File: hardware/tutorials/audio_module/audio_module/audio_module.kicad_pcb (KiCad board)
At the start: 2 copper layers, 25.5 x 32 mm, 5 parts

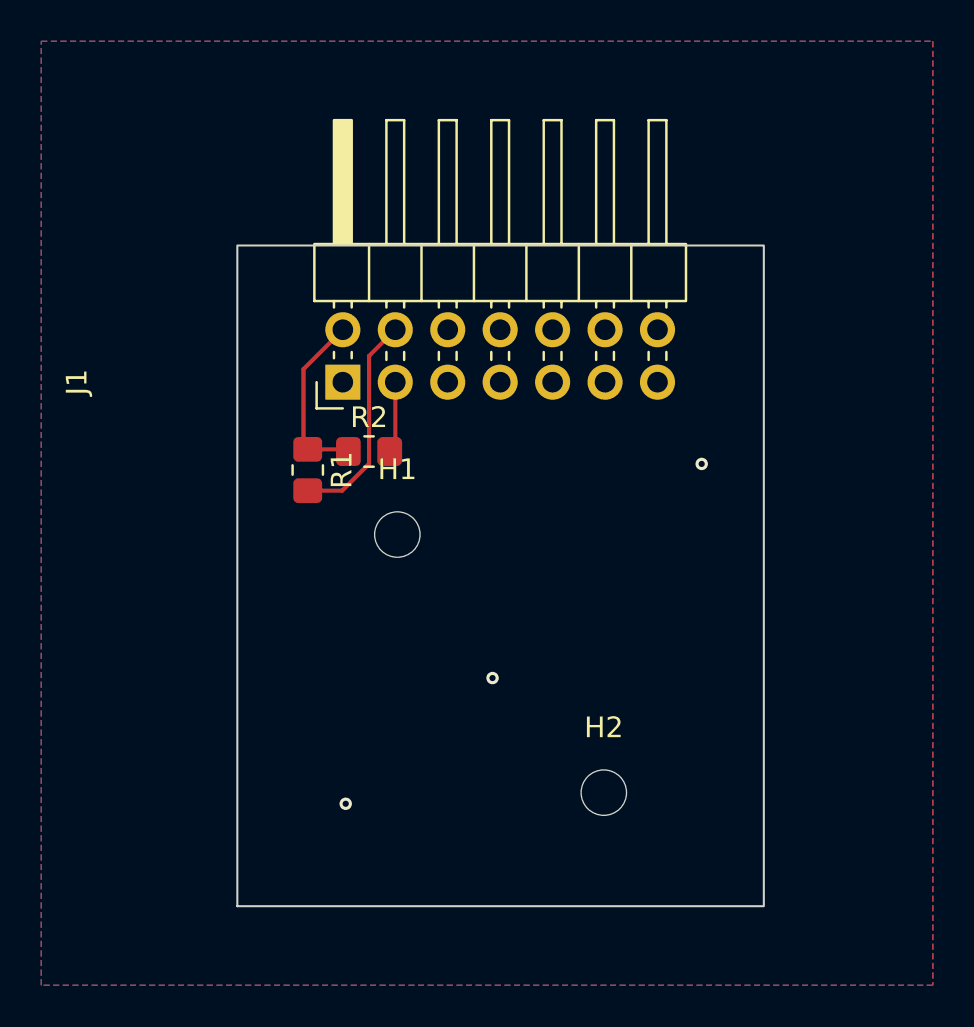
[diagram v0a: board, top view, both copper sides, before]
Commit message: started pcb layout and traces for tutorial module
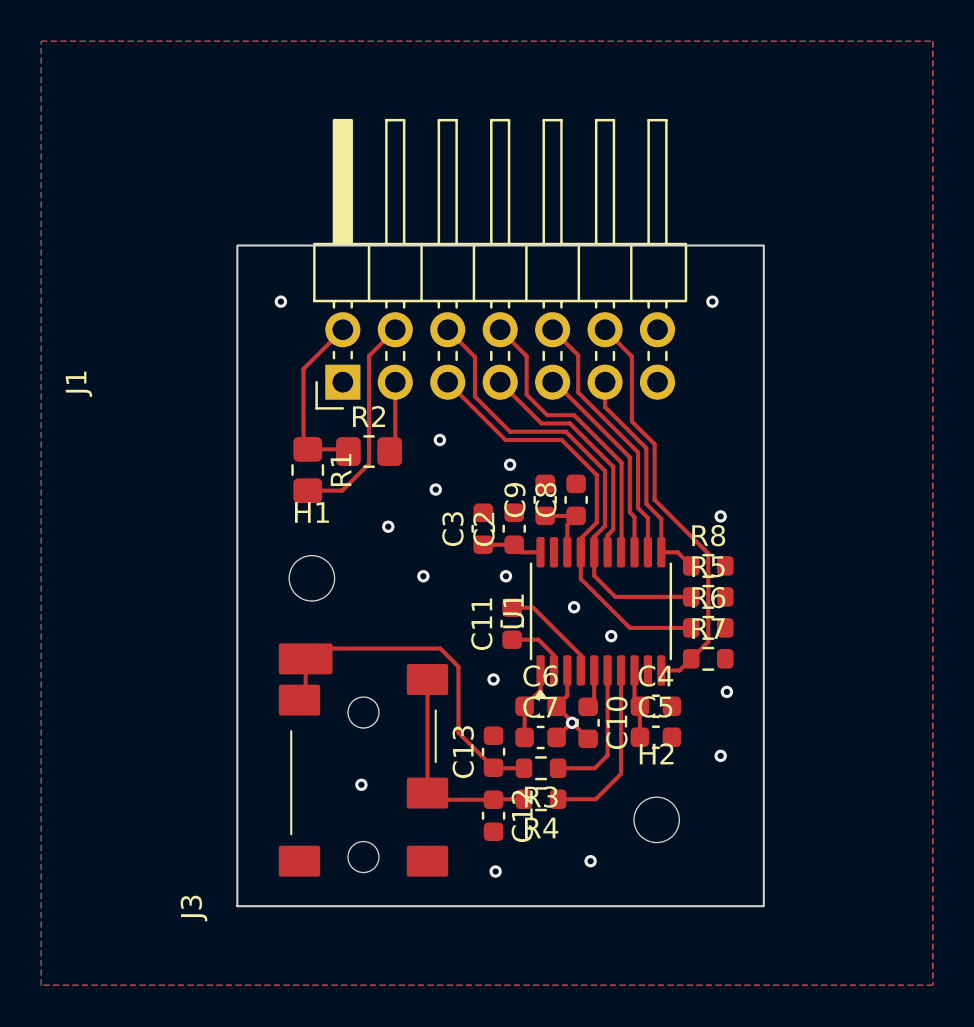
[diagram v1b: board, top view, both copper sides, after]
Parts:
- added C10: 2u2, Capacitor_SMD:C_0603_1608Metric, F.Cu at (144.9, 110.2)
- added C11: 2u2, Capacitor_SMD:C_0603_1608Metric, F.Cu at (141.2, 105.4)
- added C12: 2u2, Capacitor_SMD:C_0603_1608Metric, F.Cu at (140.3, 114.7)
- added C13: 2u2, Capacitor_SMD:C_0603_1608Metric, F.Cu at (140.3, 111.6)
- added C2: 100n, Capacitor_SMD:C_0603_1608Metric, F.Cu at (141.3, 100.8)
- added C3: 10u, Capacitor_SMD:C_0603_1608Metric, F.Cu at (139.8, 100.8)
- added C4: 100n, Capacitor_SMD:C_0603_1608Metric, F.Cu at (148.1, 109.4)
- added C5: 10u, Capacitor_SMD:C_0603_1608Metric, F.Cu at (148.1, 110.9)
- added C6: 100n, Capacitor_SMD:C_0603_1608Metric, F.Cu at (142.6, 109.4)
- added C7: 10u, Capacitor_SMD:C_0603_1608Metric, F.Cu at (142.6, 110.9)
- added C8: 100n, Capacitor_SMD:C_0603_1608Metric, F.Cu at (144.3, 99.4)
- added C9: 10u, Capacitor_SMD:C_0603_1608Metric, F.Cu at (142.8, 99.4)
- added J3: AudioJack4_SwitchTR1, audio_jack:PJ-342, F.Cu at (134.0, 119.1)
- added R3: 470R, Resistor_SMD:R_0603_1608Metric, F.Cu at (142.6, 112.4)
- added R4: 470R, Resistor_SMD:R_0603_1608Metric, F.Cu at (142.6, 113.9)
- added R5: 10k, Resistor_SMD:R_0603_1608Metric, F.Cu at (150.7, 104.1)
- added R6: 10k, Resistor_SMD:R_0603_1608Metric, F.Cu at (150.7, 105.6)
- added R7: 10k, Resistor_SMD:R_0603_1608Metric, F.Cu at (150.7, 107.1)
- added R8: 10k, Resistor_SMD:R_0603_1608Metric, F.Cu at (150.7, 102.6)
- added U1: PCM5102A, Package_SO:TSSOP-20_4.4x6.5mm_P0.65mm, F.Cu at (145.5, 104.8)
- moved H1 4.65 mm to (131.5, 103.2)
- moved H2 2.88 mm to (148.2, 114.9)
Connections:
- J1 pad 10: unconnected-(J1-GPIO5-Pad10) -> /SCK
- J1 pad 11: unconnected-(J1-GPIO6-Pad11) -> /FILTER
- J1 pad 12: unconnected-(J1-GPIO7-Pad12) -> /DEMP
- J1 pad 5: unconnected-(J1-GPIO0-Pad5) -> /MUTE
- J1 pad 6: unconnected-(J1-GPIO1-Pad6) -> /FORMAT
- J1 pad 7: unconnected-(J1-GPI02-Pad7) -> /WORDSEL
- J1 pad 8: unconnected-(J1-GPIO3-Pad8) -> /DATA
- J1 pad 9: unconnected-(J1-GPIO4-Pad9) -> /BITCLK
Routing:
- net /FORMAT: track 0.00 -> 22.0 mm
- net /MUTE: track 0.00 -> 20.8 mm
- net /DEMP: track 0.00 -> 20.0 mm
- net /OUTL: track 0.00 -> 17.2 mm
- net /DATA: track 0.00 -> 14.0 mm
- net /SCK: track 0.00 -> 12.7 mm
- net /WORDSEL: track 0.00 -> 11.4 mm
- net /FILTER: track 0.00 -> 11.1 mm
- net /OUTR: track 0.00 -> 10.3 mm
- net /BITCLK: track 0.00 -> 9.94 mm
- net Net-(U1-OUTR): track 0.00 -> 8.57 mm
- net VDDA: track 0.00 -> 6.91 mm
- net Net-(U1-OUTL): track 0.00 -> 6.77 mm
- net GND: track 0.00 -> 5.20 mm, vias 3 -> 18
- net Net-(U1-CAPM): track 0.00 -> 5.02 mm
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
